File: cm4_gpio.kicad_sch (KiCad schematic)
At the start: 35 parts, among them CN7 104031-0811, U8 SN74LVC1G125DBV

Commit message: Added M.2 SSD
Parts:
- CN4: MPN DF40C-100DS-0.4V -> DF40C-100DS-0.4V(51)
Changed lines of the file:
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@@
     )
   )
-  (symbol (lib_name "ComputeModule4-GPIO_1") (lib_id "Modules_WUT:ComputeModule4-GPIO") (at 105.41 39.37 0) (unit 4)
+  (symbol (lib_id "Modules_WUT:ComputeModule4-GPIO") (at 105.41 39.37 0) (unit 4)
     (in_bom yes) (on_board yes) (dnp no) (fields_autoplaced)
     (property "Reference" "CN4" (at 105.41 34.29 0)
@@
       (effects (font (size 1.27 1.27)) hide)
     )
-    (property "MPN" "DF40C-100DS-0.4V" (at 105.41 39.37 0)
+    (property "MPN" "DF40C-100DS-0.4V(51)" (at 105.41 39.37 0)
       (effects (font (size 1.27 1.27)) hide)
     )
@@
       (effects (font (size 1.27 1.27)) hide)
     )
-    (property "MPN" "DF40C-100DS-0.4V" (at 209.55 111.76 0)
+    (property "MPN" "DF40C-100DS-0.4V(51)" (at 209.55 111.76 0)
       (effects (font (size 1.27 1.27)) hide)
     )
@@
       (effects (font (size 1.27 1.27)) hide)
     )
-    (property "MPN" "DF40C-100DS-0.4V" (at 71.12 148.59 0)
-      (effects (font (size 1.27 1.27)) hide)
-    )
+    (property "MPN" "DF40C-100DS-0.4V(51)" (at 71.12 148.59 0)
+      (effects (font (size 1.27 1.27)) hide)
+    )

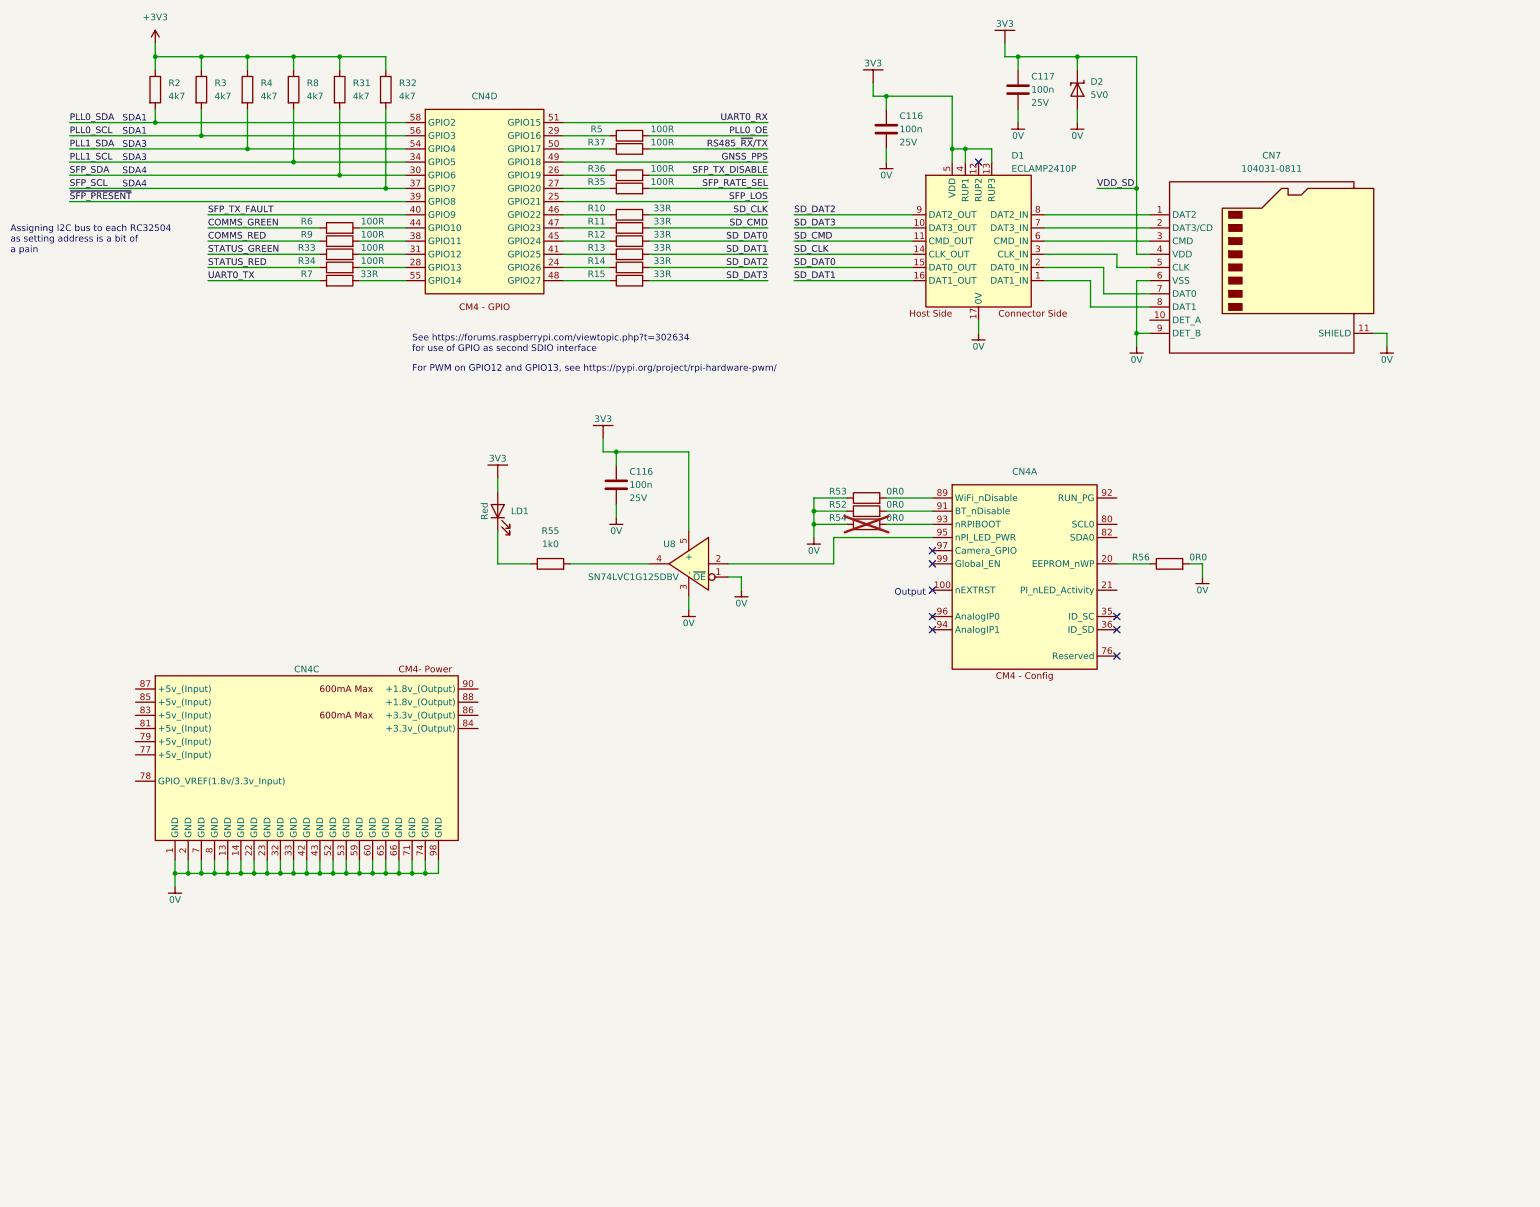
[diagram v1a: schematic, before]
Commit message: Added ESD and tided up PSU
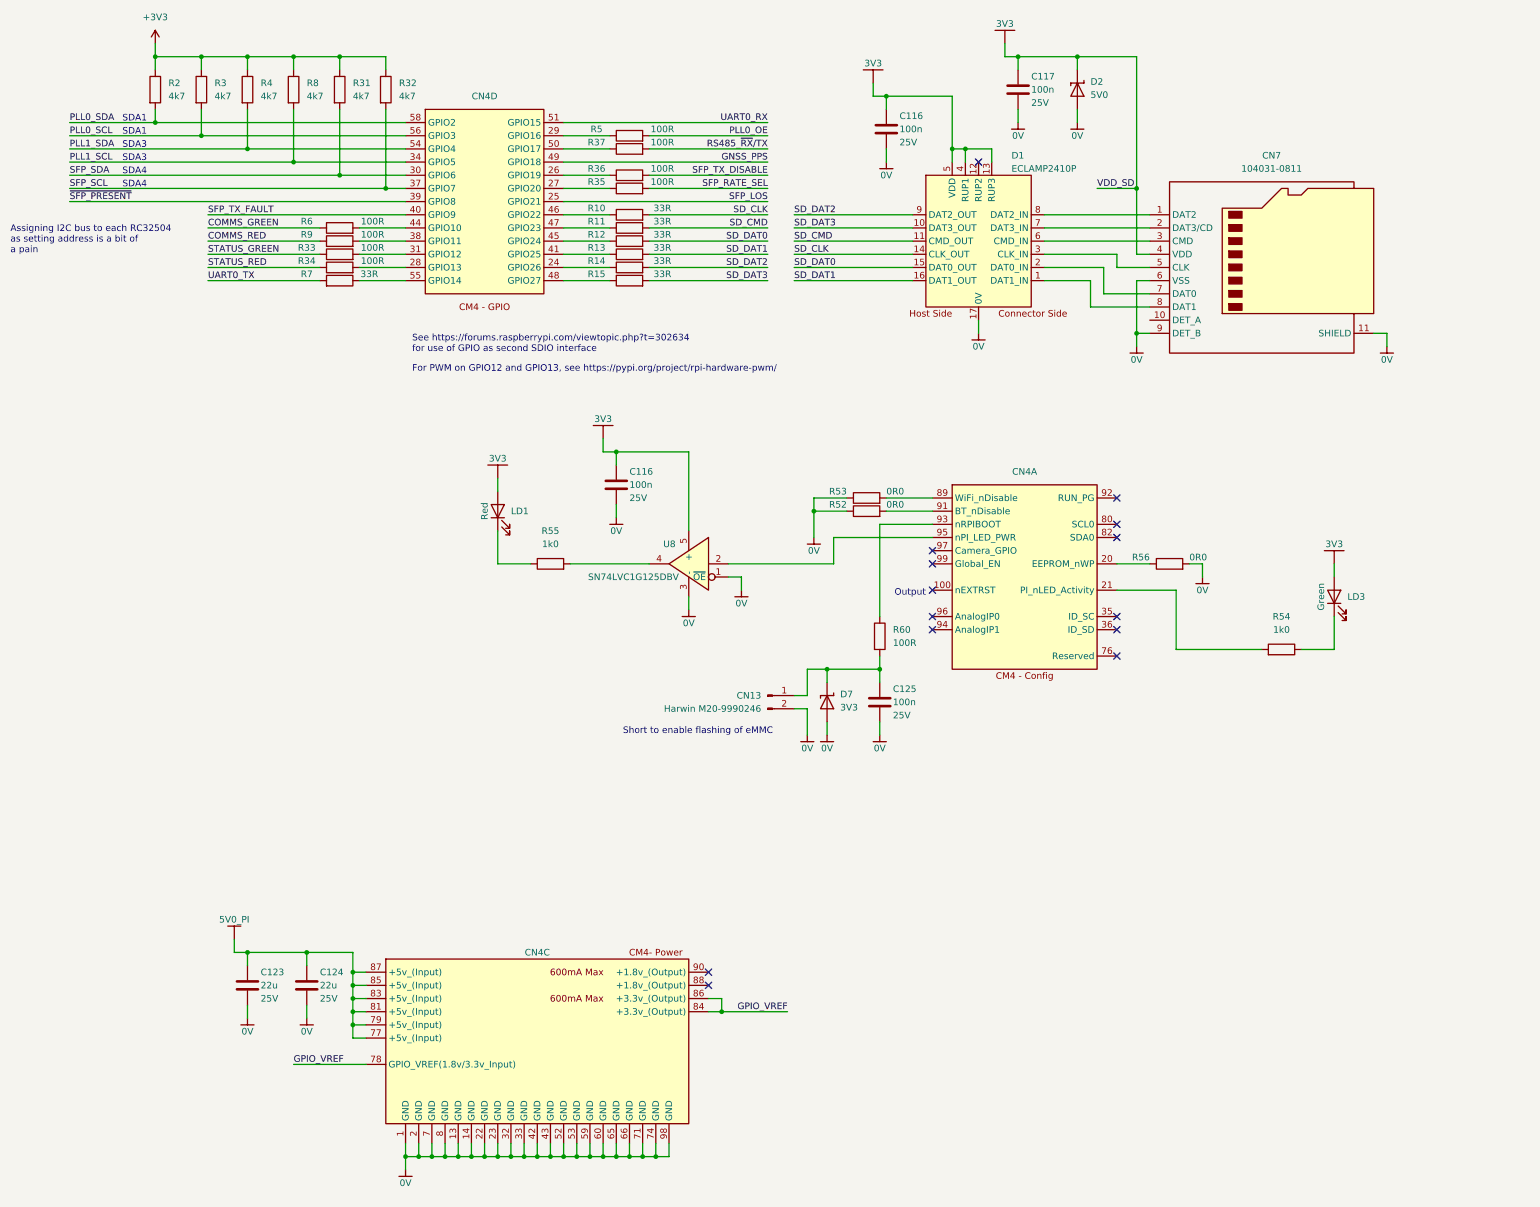
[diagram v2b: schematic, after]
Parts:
- removed R54: 0R0, Resistor_SMD:R_0402_1005Metric, symbol Auto_Library_WUT:KOA Speer RK73Z1ETTP
- added C123, C124: 22u, Capacitor_SMD:C_1206_3216Metric, symbol Auto_Library_WUT:Kyocera AVX 12063D226KAT2A
- added C125: 100n, Capacitor_SMD:C_0402_1005Metric, symbol Auto_Library_WUT:Yageo CC0402KRX7R8BB104
- added CN13: Harwin M20-9990246, Connector_PinHeader_2.54mm:PinHeader_1x02_P2.54mm_Vertical, symbol Connector_WUT:Harwin_M20-9990246
- added D7: 3V3, Diode_SMD:D_SOD-523, symbol Auto_Library_WUT:nexperia PESD3V3U1UB,115
- added LD3: Green, LED_SMD:LED_0603_1608Metric, symbol Auto_Library_WUT:Ekinglux_E6C0603VGAC1UDA
- added R54: 1k0, Resistor_SMD:R_0402_1005Metric, symbol Auto_Library_WUT:KOA Speer RK73H1ETTP1001F
- added R60: 100R, Resistor_SMD:R_0402_1005Metric, symbol Auto_Library_WUT:KOA Speer RK73H1ETTP1000F
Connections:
- net 0V: now also C123.2, C124.2, C125.2, CN13.2 (Pin_2), D7.2 (A)
- net 3V3: now also LD3.2 (A)
- net at CN4.21 (PI_nLED_Activity): now also R54.2
- net at CN4.93 (nRPIBOOT): now also R60.1
- net 5V0_PI: now reaches CN4.77 (+5v_(Input))
- net 5V0_PI: now also CN4.79 (+5v_(Input)), CN4.81 (+5v_(Input)), CN4.83 (+5v_(Input)), CN4.85 (+5v_(Input)), CN4.87 (+5v_(Input)), C123.1, C124.1
- net GPIO_VREF: now reaches CN4.78 (GPIO_VREF(1.8v/3.3v_Input))
- net GPIO_VREF: now also CN4.84 (+3.3v_(Output)), CN4.86 (+3.3v_(Output))
- new net: LD3.1 (K), R54.1
- new net: C125.1, CN13.1 (Pin_1), D7.1 (K), R60.2
- no-connect marks 9 -> 14
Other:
- note added: "Short to enable flashing of eMMC"
- moved on the sheet: CN4C

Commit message: started on power
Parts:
- CN7: footprint Connector_Card:microSD_HC_Molex_104031-0811 -> Connector_WUT:microSD_HC_Molex_104031-0811
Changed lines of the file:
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@@
       (effects (font (size 1.27 1.27)))
     )
-    (property "Footprint" "Connector_Card:microSD_HC_Molex_104031-0811" (at 257.81 66.04 0)
+    (property "Footprint" "Connector_WUT:microSD_HC_Molex_104031-0811" (at 257.81 66.04 0)
       (effects (font (size 1.27 1.27)) hide)
     )

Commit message: Added power supply
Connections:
- net GPIO_VREF is gone; now on net 3V3: CN4.78 (GPIO_VREF(1.8v/3.3v_Input)), CN4.84 (+3.3v_(Output)), CN4.86 (+3.3v_(Output))
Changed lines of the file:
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@@
     (stroke (width 0) (type default))
   )
+  (wire (pts (xy 154.94 207.01) (xy 154.94 210.82))
+    (stroke (width 0) (type default))
+  )
   (wire (pts (xy 59.69 26.67) (xy 59.69 29.21))
     (stroke (width 0) (type default))
@@
     (stroke (width 0) (type default))
   )
-  (wire (pts (xy 68.58 220.98) (xy 82.55 220.98))
+  (wire (pts (xy 76.2 220.98) (xy 82.55 220.98))
     (stroke (width 0) (type default))
   )
@@
     (stroke (width 0) (type default))
   )
+  (wire (pts (xy 76.2 220.98) (xy 76.2 219.71))
+    (stroke (width 0) (type default))
+  )
   (wire (pts (xy 82.55 213.36) (xy 80.01 213.36))
     (stroke (width 0) (type default))
@@
     (stroke (width 0) (type default))
   )
-  (wire (pts (xy 151.13 210.82) (xy 163.83 210.82))
+  (wire (pts (xy 151.13 210.82) (xy 154.94 210.82))
     (stroke (width 0) (type default))
   )
@@
     (effects (font (size 1.27 1.27)) (justify left bottom))
   )
-  (label "GPIO_VREF" (at 163.83 210.82 180) (fields_autoplaced)
-    (effects (font (size 1.27 1.27)) (justify right bottom))
-  )
   (label "SFP_TX_DISABLE" (at 160.02 49.53 180) (fields_autoplaced)
     (effects (font (size 1.27 1.27)) (justify right bottom))
@@
     (effects (font (size 1.27 1.27)) (justify right bottom))
   )
-  (label "GPIO_VREF" (at 68.58 220.98 0) (fields_autoplaced)
-    (effects (font (size 1.27 1.27)) (justify left bottom))
-  )
   (netclass_flag "" (length 1.27) (shape round) (at 177.8 62.23 0) (fields_autoplaced)
     (effects (font (size 1.27 1.27)) (justify left bottom))
@@
     )
   )
+  (symbol (lib_id "Power_WUT:3V3") (at 76.2 219.71 0) (unit 1)
+    (in_bom no) (on_board no) (dnp no) (fields_autoplaced)
+    (property "Reference" "#PWR0244" (at 75.565 222.885 0)
+      (effects (font (size 1.27 1.27)) hide)
+    )
+    (property "Value" "3V3" (at 76.2 215.9 0) (do_not_autoplace)
+      (effects (font (size 1.27 1.27)))
+    )
+    (property "Footprint" "" (at 76.2 219.71 0)
+      (effects (font (size 1.27 1.27)) hide)
+    )
+    (property "Datasheet" "" (at 76.2 219.71 0)
+      (effects (font (size 1.27 1.27)) hide)
+    )
+    (pin "1")
+    (instances
+      (project "Master Timing Card"
+        (path "/6e8e281e-e30f-459d-852f-231836068db5/3fdc825c-420f-4918-ada8-75992123f8b4"
+          (reference "#PWR0244") (unit 1)
+        )
+      )
+    )
+  )
   (symbol (lib_id "Auto_Library_WUT:KOA Speer RK73H1ETTP33R0F") (at 133.35 67.31 90) (unit 1)
     (in_bom yes) (on_board yes) (dnp no)
@@
         )
       )
+    )
+  )
+  (symbol (lib_id "Power_WUT:3V3") (at 154.94 207.01 0) (unit 1)
+    (in_bom no) (on_board no) (dnp no) (fields_autoplaced)
+    (property "Reference" "#PWR0243" (at 154.305 210.185 0)
+      (effects (font (size 1.27 1.27)) hide)
+    )
+    (property "Value" "3V3" (at 154.94 203.2 0) (do_not_autoplace)
+      (effects (font (size 1.27 1.27)))
+    )
+    (property "Footprint" "" (at 154.94 207.01 0)
+      (effects (font (size 1.27 1.27)) hide)
+    )
+    (property "Datasheet" "" (at 154.94 207.01 0)
+      (effects (font (size 1.27 1.27)) hide)
+    )
+    (pin "1")
+    (instances
+      (project "Master Timing Card"
+        (path "/6e8e281e-e30f-459d-852f-231836068db5/3fdc825c-420f-4918-ada8-75992123f8b4"
+          (reference "#PWR0243") (unit 1)
+        )
+      )

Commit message: Schematic mostly done
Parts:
- removed C116, C117: 100n, Capacitor_SMD:C_0402_1005Metric, symbol Auto_Library_WUT:Yageo CC0402KRX7R8BB104
- removed CN7: 104031-0811, Connector_WUT:microSD_HC_Molex_104031-0811, symbol Connector_WUT:Molex_104031-0811
- removed D1: ECLAMP2410P, Diode_WUT:Semtech_ECLAMP2410P, symbol Diode_WUT:Semtech_EClamp2410P
- removed D2: 5V0, Diode_SMD:D_SOD-323, symbol Auto_Library_WUT:nexperia PESD5V0U1UA,115
- removed R10, R11, R12, R13, R14, R15: 33R, Resistor_SMD:R_0402_1005Metric, symbol Auto_Library_WUT:KOA Speer RK73H1ETTP33R0F
- removed R35: 100R, Resistor_SMD:R_0402_1005Metric, symbol Auto_Library_WUT:KOA Speer RK73H1ETTP1000F
- removed R8: 4k7, Resistor_SMD:R_0402_1005Metric, symbol Auto_Library_WUT:KOA Speer RK73H1ETTP4701F
- added C158: 1u, Capacitor_SMD:C_0402_1005Metric, symbol Auto_Library_WUT:Kemet C0402C105K4PACTU
- added R117, R35: 4k7, Resistor_SMD:R_0402_1005Metric, symbol Auto_Library_WUT:KOA Speer RK73H1ETTP4701F
- added R130, R131: 6R8, Resistor_SMD:R_0402_1005Metric, symbol Auto_Library_WUT:KOA Speer RK73H1ETTP6R80F
- added R14, R8: 100R, Resistor_SMD:R_0402_1005Metric, symbol Auto_Library_WUT:KOA Speer RK73H1ETTP1000F
- added R15: 150m, Resistor_SMD:R_0603_1608Metric, symbol Auto_Library_WUT:Panasonic ERJ3RSFR15V
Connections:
- net +3V3 is gone; now on net 3V3: R2.1, R3.1, R31.1, R32.1, R4.1
- net PLL0_SCL is gone; now on net PLL1_SCL: CN4.56 (GPIO3), R3.2
- net PLL0_SDA is gone; now on net PLL1_SDA: CN4.58 (GPIO2), R2.2
- net 3V3: now also R117.1, R130.1, R15.2, R35.1; no longer CN4.84 (+3.3v_(Output)), CN4.86 (+3.3v_(Output))
- net PLL1_SCL: no longer CN4.34 (GPIO5)
- net PLL1_SDA: no longer CN4.54 (GPIO4), R4.2
- net SFP_LOS: now also R35.2
- net SFP_TX_FAULT: now also R4.2
- net ~{SFP_PRESENT}: now also R117.2
- net PCIE_PWR_GOOD: now reaches CN4.45 (GPIO24)
- net PLL_LOCK: now reaches CN4.27 (GPIO20)
- net at CN4.41 (GPIO25): now also R14.1
- net at CN4.46 (GPIO22): now also R8.1
- net PWR_CRITICAL: now reaches CN4.47 (GPIO23)
- net 1V8: now reaches CN4.88 (+1.8v_(Output))
- net 1V8: now also CN4.90 (+1.8v_(Output))
- net PLL0_OE renamed PLL_OE
- net SFP_SCL renamed PLL2_SCL
- net SFP_SDA renamed PLL2_SDA
- new net: CN4.84 (+3.3v_(Output)), CN4.86 (+3.3v_(Output)), R131.1, R15.1
- new net 3V3_PCIE_EN: R8.2
- new net 3V3_SENSE_N: C158.1, R130.2
- new net 3V3_SENSE_P: C158.2, R131.2
- new net GNSS_RESET: R14.2
- new net UART3_RX: CN4.34 (GPIO5)
- new net UART3_TX: CN4.54 (GPIO4)
- no-connect marks 14 -> 13
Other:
- note added: "I2C1"
- note added: "I2C4"
- note added: "Imax = 600mA Max drop = 0.6 * 0.15 = 90mV Power = 0.6^2 * 0.15 = 54mW"
- note added: "UART3"
- note removed: "SDA1"
- note removed: "SDA3"
- note removed: "SDA4"
- moved on the sheet: R2, R3, R31, R32

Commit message: schematic complete
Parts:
- added R136, R24: 100R, Resistor_SMD:R_0402_1005Metric, symbol Auto_Library_WUT:KOA Speer RK73H1ETTP1000F
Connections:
- net at CN4.24 (GPIO26): now also R24.1
- net at CN4.48 (GPIO27): now also R136.1
- new net PLL_CLK_SEL: R136.2
- new net REF_CLK_SEL: R24.2
- no-connect marks 13 -> 11
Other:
- moved on the sheet: C116, C123, C124, C125, C158, CN13, CN4A, CN4C, CN4D, D7, LD1, LD3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
